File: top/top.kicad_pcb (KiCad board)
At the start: 4 copper layers, 28.3 x 40 mm, 23 parts, among them P1 CONN_10, P2 CONN_5, P3 CONN_20, U1 IQS572, U4 ESD

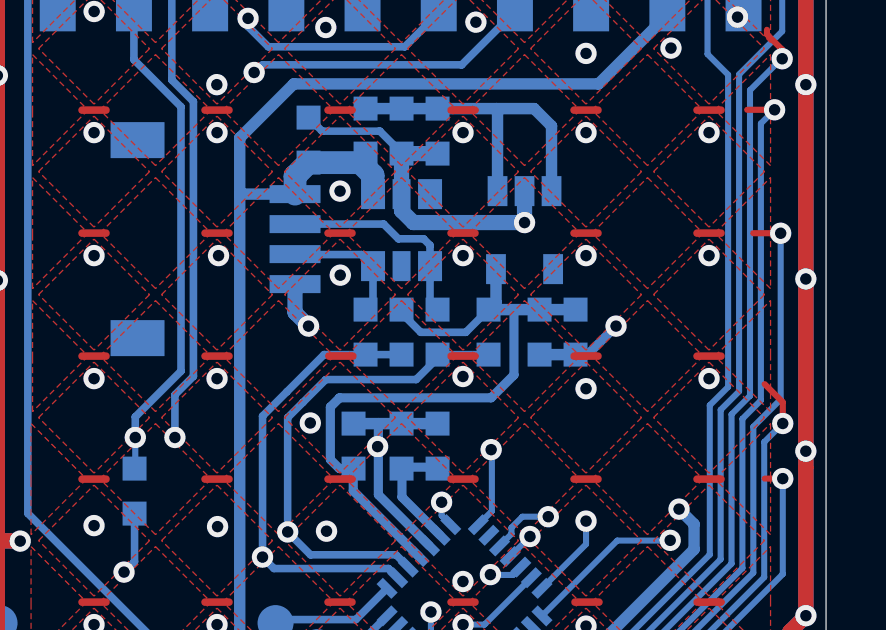
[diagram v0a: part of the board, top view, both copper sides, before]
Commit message: Remove redundant I2C pull-up resistors.
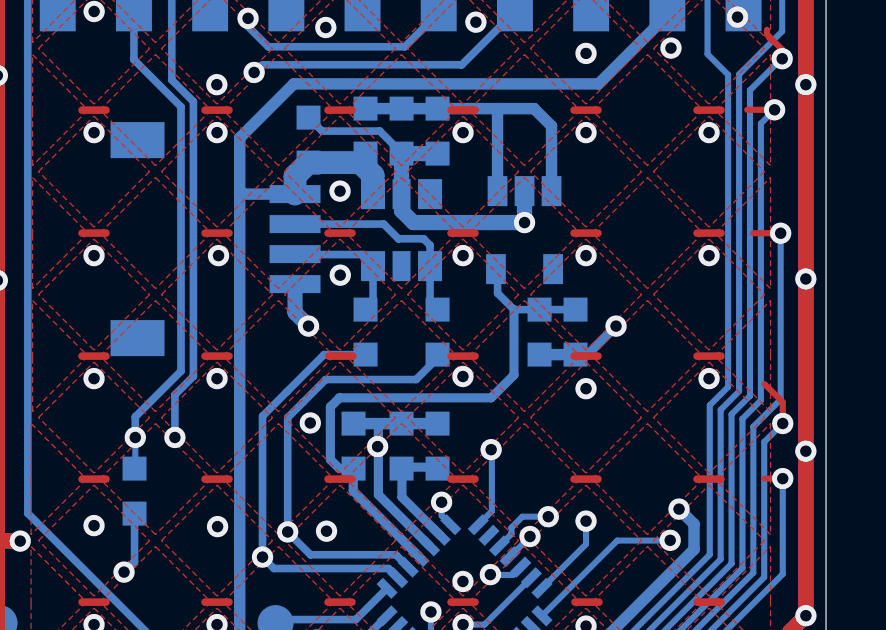
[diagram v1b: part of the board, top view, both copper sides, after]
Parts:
- removed R1, R2: 2.2K, ugl:SM0603
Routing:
- net +3V3: track 23.3 -> 18.4 mm
- net /SCL: track 56.0 -> 54.3 mm
- net /SDA: track 52.8 -> 51.4 mm
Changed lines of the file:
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@@
-(kicad_pcb (version 20171130) (host pcbnew 5.1.5-52549c5~84~ubuntu18.04.1)
+(kicad_pcb (version 20171130) (host pcbnew 5.1.5-52549c5~86~ubuntu18.04.1)
   (general
     (thickness 1.6)
     (drawings 75)
-    (tracks 759)
+    (tracks 756)
     (zones 0)
-    (modules 23)
+    (modules 21)
     (nets 53)
   )
@@
   )
   (layers
-    (0 F.Cu mixed hide)
+    (0 F.Cu mixed)
     (1 In1.Cu signal hide)
     (2 In2.Cu signal hide)
@@
     (46 B.CrtYd user)
     (47 F.CrtYd user)
-    (48 B.Fab user hide)
-    (49 F.Fab user hide)
+    (48 B.Fab user)
+    (49 F.Fab user)
   )
   (setup
-    (last_trace_width 0.2032)
+    (last_trace_width 0.254)
     (user_trace_width 0.2032)
     (user_trace_width 0.254)
@@
     (pad 2 smd rect (at 0.75 0 270) (size 0.8 0.8) (layers B.Cu B.Paste B.Mask)
       (net 4 /VCC_BOTTOM))
-    (model smd\resistors\R0603.wrl
-      (offset (xyz 0 0 0.02540000082496551))
-      (scale (xyz 0.5 0.5 0.5))
-      (rotate (xyz 0 0 0))
-    )
-  )
-  (module ugl:SM0603 (layer B.Cu)
-    (at 208.6 141.7 90)
-    (attr smd)
-    (fp_text reference R1 (at -3.08 1.8898 180) (layer B.SilkS)
-      (effects (font (size 0.75 0.75) (thickness 0.15)) (justify mirror))
-    )
-    (fp_text value 2.2K (at -4.2 2.4) (layer B.SilkS)
-      (effects (font (size 0.75 0.75) (thickness 0.15)) (justify mirror))
-    )
-    (fp_line (start 0.4 -0.5) (end -0.4 -0.5) (layer B.SilkS) (width 0.127))
-    (fp_line (start -0.4 0.5) (end 0.4 0.5) (layer B.SilkS) (width 0.127))
-    (pad 2 smd rect (at 0.75 0 90) (size 0.8 0.8) (layers B.Cu B.Paste B.Mask)
-      (net 12 +3V3))
-    (pad 1 smd rect (at -0.75 0 90) (size 0.8 0.8) (layers B.Cu B.Paste B.Mask)
-      (net 8 /SCL))
-    (model smd\resistors\R0603.wrl
-      (offset (xyz 0 0 0.02540000082496551))
-      (scale (xyz 0.5 0.5 0.5))
-      (rotate (xyz 0 0 0))
-    )
-  )
-  (module ugl:SM0603 (layer B.Cu)
-    (at 205.7 141.7 90)
-    (attr smd)
-    (fp_text reference R2 (at -3.7404 -6.6 270) (layer B.SilkS)
-      (effects (font (size 0.75 0.75) (thickness 0.15)) (justify mirror))
-    )
-    (fp_text value 2.2K (at -6.3 -6.6 90) (layer B.SilkS)
-      (effects (font (size 0.75 0.75) (thickness 0.15)) (justify mirror))
-    )
-    (fp_line (start -0.4 0.5) (end 0.4 0.5) (layer B.SilkS) (width 0.127))
-    (fp_line (start 0.4 -0.5) (end -0.4 -0.5) (layer B.SilkS) (width 0.127))
-    (pad 1 smd rect (at -0.75 0 90) (size 0.8 0.8) (layers B.Cu B.Paste B.Mask)
-      (net 11 /SDA))
-    (pad 2 smd rect (at 0.75 0 90) (size 0.8 0.8) (layers B.Cu B.Paste B.Mask)
-      (net 12 +3V3))
     (model smd\resistors\R0603.wrl
       (offset (xyz 0 0 0.02540000082496551))
@@
   (segment (start 200.25 131.55) (end 200.9 130.9) (width 0.2032) (layer In2.Cu) (net 8))
   (via (at 198.0946 157.8356) (size 0.635) (drill 0.381) (layers F.Cu B.Cu) (net 8))
-  (segment (start 208.6 142.45) (end 206.9 142.45) (width 0.254) (layer B.Cu) (net 8))
   (via (at 201.9046 148.3614) (size 0.7112) (drill 0.381) (layers F.Cu B.Cu) (net 8))
   (segment (start 198.57 157.5126) (end 198.0946 157.988) (width 0.3048) (layer B.Cu) (net 8))
@@
   (segment (start 198.57 156.1664) (end 198.0184 156.718) (width 0.3048) (layer B.Cu) (net 11))
   (segment (start 198.57 156.165) (end 198.57 156.1664) (width 0.3048) (layer B.Cu) (net 11))
-  (segment (start 205.7 142.45) (end 203.117 142.45) (width 0.254) (layer B.Cu) (net 11))
   (segment (start 203.117 142.45) (end 201.8792 143.6878) (width 0.254) (layer B.Cu) (net 11))
   (segment (start 201.0664 144.5006) (end 201.0664 149.1996) (width 0.254) (layer B.Cu) (net 11))
@@
   (segment (start 201.0664 133.3246) (end 200.787 133.0452) (width 0.254) (layer In1.Cu) (net 11))
   (segment (start 201.0664 149.1996) (end 201.0664 133.3246) (width 0.254) (layer In1.Cu) (net 11))
-  (segment (start 208.8475 140.7025) (end 208.6 140.95) (width 0.381) (layer B.Cu) (net 12))
-  (segment (start 208.8475 139.6) (end 208.8475 140.7025) (width 0.381) (layer B.Cu) (net 12))
-  (segment (start 205.7 141.066602) (end 206.339998 141.7066) (width 0.254) (layer B.Cu) (net 12))
-  (segment (start 205.7 140.95) (end 205.7 141.066602) (width 0.254) (layer B.Cu) (net 12))
-  (segment (start 207.8434 141.7066) (end 208.6 140.95) (width 0.254) (layer B.Cu) (net 12))
-  (segment (start 206.339998 141.7066) (end 207.8434 141.7066) (width 0.254) (layer B.Cu) (net 12))
+  (segment (start 203.117 142.45) (end 204.25 142.45) (width 0.254) (layer B.Cu) (net 11))
+  (segment (start 204.25 142.45) (end 204.3 142.5) (width 0.254) (layer B.Cu) (net 11))
   (segment (start 204.089 146.989) (end 206.27972 149.17972) (width 0.3048) (layer B.Cu) (net 12))
   (segment (start 204.089 146.177) (end 204.089 146.989) (width 0.3048) (layer B.Cu) (net 12))
@@
   (segment (start 208.6864 143.891) (end 203.6318 143.891) (width 0.3048) (layer B.Cu) (net 12))
   (segment (start 209.4484 143.129) (end 209.4484 140.95) (width 0.3048) (layer B.Cu) (net 12))
-  (segment (start 211.45 140.95) (end 209.4484 140.95) (width 0.381) (layer B.Cu) (net 12))
-  (segment (start 209.4484 140.95) (end 208.6 140.95) (width 0.381) (layer B.Cu) (net 12))
+  (segment (start 209.4484 140.95) (end 210.05 140.95) (width 0.254) (layer B.Cu) (net 12))
+  (segment (start 210.05 140.95) (end 210.1 140.9) (width 0.254) (layer B.Cu) (net 12))
+  (segment (start 209.4484 140.95) (end 208.9 140.4016) (width 0.254) (layer B.Cu) (net 12))
+  (segment (start 208.9 140.4016) (end 208.9 140) (width 0.254) (layer B.Cu) (net 12))
+  (segment (start 210.3 140.95) (end 211.45 140.95) (width 0.254) (layer B.Cu) (net 12))
   (segment (start 206.9146 146.2024) (end 205.7146 146.2024) (width 0.3048) (layer B.Cu) (net 14))
   (segment (start 205.7146 147.200387) (end 205.7146 146.2278) (width 0.3048) (layer B.Cu) (net 14))

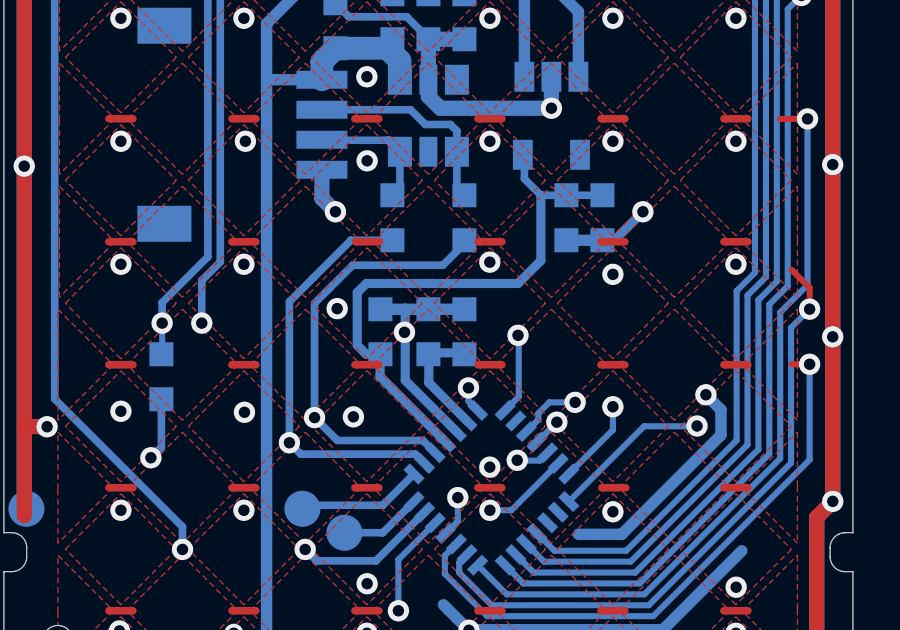
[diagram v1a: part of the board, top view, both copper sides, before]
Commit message: Move bypass caps closer to pin 4.
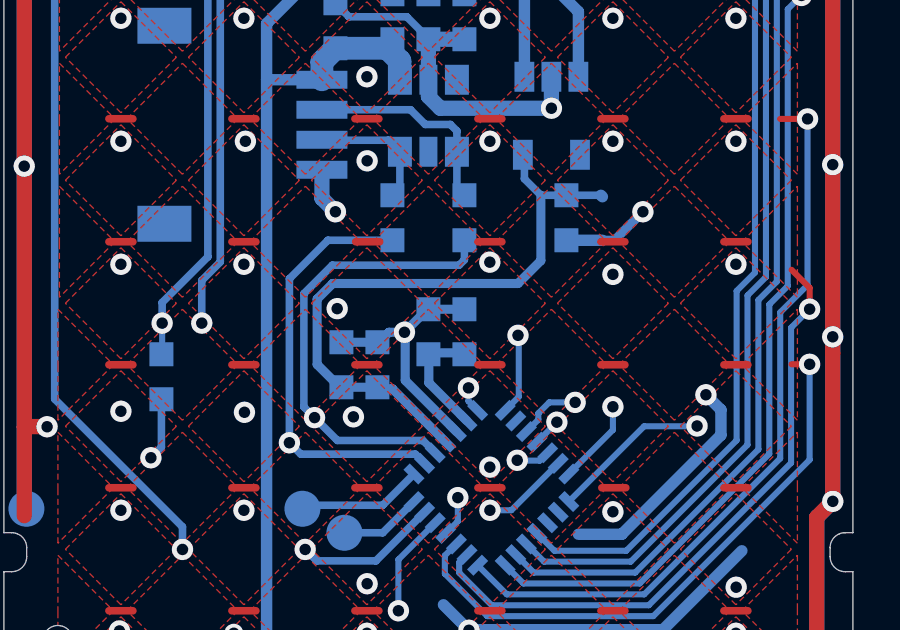
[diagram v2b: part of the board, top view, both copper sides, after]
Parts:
- moved C6 9.98 mm to (202.8, 146.6), turned to 270 degrees
- moved C5 1.10 mm to (204.0, 146.6)
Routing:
- net +3V3: track 18.4 -> 20.4 mm
- net /SCL: track 54.3 -> 55.3 mm
- net GND: track 449.5 -> 450.1 mm
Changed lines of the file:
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@@
     (thickness 1.6)
     (drawings 75)
-    (tracks 756)
+    (tracks 759)
     (zones 0)
     (modules 21)
@@
   )
   (setup
-    (last_trace_width 0.254)
+    (last_trace_width 0.3048)
     (user_trace_width 0.2032)
     (user_trace_width 0.254)
@@
   )
   (module ugl:SM0603 (layer B.Cu)
-    (at 204.1 145.5 270)
+    (at 204 146.6 270)
     (attr smd)
     (fp_text reference C5 (at 0.6262 2.17 270) (layer B.SilkS)
@@
   )
   (module ugl:SM0603 (layer B.Cu)
-    (at 211.5 141.7 90)
+    (at 202.8 146.6 270)
     (attr smd)
     (fp_text reference C6 (at 1.3 1.1742 270) (layer B.SilkS)
@@
     (fp_line (start -0.4 0.5) (end 0.4 0.5) (layer B.SilkS) (width 0.127))
     (fp_line (start 0.4 -0.5) (end -0.4 -0.5) (layer B.SilkS) (width 0.127))
-    (pad 1 smd rect (at -0.75 0 90) (size 0.8 0.8) (layers B.Cu B.Paste B.Mask)
-      (net 1 GND))
-    (pad 2 smd rect (at 0.75 0 90) (size 0.8 0.8) (layers B.Cu B.Paste B.Mask)
+    (pad 1 smd rect (at -0.75 0 270) (size 0.8 0.8) (layers B.Cu B.Paste B.Mask)
+      (net 1 GND))
+    (pad 2 smd rect (at 0.75 0 270) (size 0.8 0.8) (layers B.Cu B.Paste B.Mask)
       (net 12 +3V3))
     (model smd\resistors\R0603.wrl
@@
   (segment (start 204.9272 147.120093) (end 204.9272 145.288) (width 0.3048) (layer B.Cu) (net 1))
   (segment (start 206.633274 148.826167) (end 204.9272 147.120093) (width 0.3048) (layer B.Cu) (net 1))
-  (segment (start 204.5 144.75) (end 204.9272 144.75) (width 0.381) (layer B.Cu) (net 1))
   (via (at 204.9018 145.5166) (size 0.7112) (drill 0.381) (layers F.Cu B.Cu) (net 1))
-  (segment (start 204.9272 144.75) (end 206.9 144.75) (width 0.381) (layer B.Cu) (net 1))
-  (segment (start 204.9272 144.7546) (end 204.9018 144.7292) (width 0.3048) (layer B.Cu) (net 1))
-  (segment (start 204.9272 145.288) (end 204.9272 144.7546) (width 0.3048) (layer B.Cu) (net 1))
   (segment (start 192.2272 121.412) (end 192.2272 122.0724) (width 0.508) (layer B.Cu) (net 1))
   (segment (start 194.4878 119.1514) (end 192.2272 121.412) (width 0.508) (layer B.Cu) (net 1))
@@
   (segment (start 214.95 147.6) (end 214.95 147.6) (width 0.381) (layer B.Cu) (net 1))
   (via (at 214.95 147.6) (size 0.7112) (drill 0.381) (layers F.Cu B.Cu) (net 1))
+  (segment (start 204.3834 145.5166) (end 204.3 145.6) (width 0.3048) (layer B.Cu) (net 1))
+  (segment (start 204.9018 145.5166) (end 205.4 145.0184) (width 0.3048) (layer B.Cu) (net 1))
+  (segment (start 205.7 144.75) (end 206.75 144.75) (width 0.3048) (layer B.Cu) (net 1))
+  (segment (start 206.75 144.75) (end 206.8 144.8) (width 0.3048) (layer B.Cu) (net 1))
+  (segment (start 204.9018 145.5166) (end 204.3834 145.5166) (width 0.3048) (layer B.Cu) (net 1))
+  (segment (start 202.8 145.85) (end 203.85 145.85) (width 0.3048) (layer B.Cu) (net 1))
+  (segment (start 203.85 145.85) (end 203.9 145.9) (width 0.3048) (layer B.Cu) (net 1))
   (segment (start 206.65 140.7) (end 206.9 140.95) (width 0.254) (layer B.Cu) (net 2))
   (segment (start 206.65 139.5) (end 206.65 140.7) (width 0.254) (layer B.Cu) (net 2))
@@
   (segment (start 198.57 157.5126) (end 198.0946 157.988) (width 0.3048) (layer B.Cu) (net 8))
   (segment (start 198.57 157.435) (end 198.57 157.5126) (width 0.3048) (layer B.Cu) (net 8))
-  (segment (start 206.9 142.566602) (end 206.9 142.45) (width 0.254) (layer B.Cu) (net 8))
-  (segment (start 206.185202 143.2814) (end 206.9 142.566602) (width 0.254) (layer B.Cu) (net 8))
-  (segment (start 203.1746 143.2814) (end 206.185202 143.2814) (width 0.254) (layer B.Cu) (net 8))
-  (segment (start 202.4126 144.0434) (end 203.1746 143.2814) (width 0.254) (layer B.Cu) (net 8))
-  (segment (start 201.9046 144.5514) (end 201.9046 148.3614) (width 0.254) (layer B.Cu) (net 8))
-  (segment (start 202.4126 144.0434) (end 201.9046 144.5514) (width 0.254) (layer B.Cu) (net 8))
   (segment (start 202.6666 149.1234) (end 201.9046 148.3614) (width 0.254) (layer B.Cu) (net 8))
   (segment (start 205.926167 149.533274) (end 205.516293 149.1234) (width 0.254) (layer B.Cu) (net 8))
@@
   (segment (start 200.8378 155.855698) (end 200.8378 150.7744) (width 0.254) (layer In1.Cu) (net 8))
   (segment (start 200.8378 150.7744) (end 201.9046 149.7076) (width 0.254) (layer In1.Cu) (net 8))
+  (segment (start 201.549001 148.005801) (end 201.549001 144.229127) (width 0.254) (layer B.Cu) (net 8))
+  (segment (start 201.549001 144.229127) (end 202.496728 143.2814) (width 0.254) (layer B.Cu) (net 8))
+  (segment (start 201.9046 148.3614) (end 201.549001 148.005801) (width 0.254) (layer B.Cu) (net 8))
+  (segment (start 202.496728 143.2814) (end 206.7226 143.2814) (width 0.254) (layer B.Cu) (net 8))
+  (segment (start 206.7226 143.2814) (end 206.9 143.104) (width 0.254) (layer B.Cu) (net 8))
+  (segment (start 206.9 143.104) (end 206.9 142.45) (width 0.254) (layer B.Cu) (net 8))
   (segment (start 208.9 134.2748) (end 208.9 137) (width 0.381) (layer B.Cu) (net 9))
   (segment (start 204.5 134.25) (end 208.8752 134.25) (width 0.381) (layer B.Cu) (net 9))
@@
   (segment (start 198.57 156.1664) (end 198.0184 156.718) (width 0.3048) (layer B.Cu) (net 11))
   (segment (start 198.57 156.165) (end 198.57 156.1664) (width 0.3048) (layer B.Cu) (net 11))
-  (segment (start 203.117 142.45) (end 201.8792 143.6878) (width 0.254) (layer B.Cu) (net 11))
-  (segment (start 201.0664 144.5006) (end 201.0664 149.1996) (width 0.254) (layer B.Cu) (net 11))
-  (segment (start 201.8792 143.6878) (end 201.0664 144.5006) (width 0.254) (layer B.Cu) (net 11))
   (segment (start 201.4474 149.5806) (end 201.0664 149.1996) (width 0.254) (layer B.Cu) (net 11))
   (segment (start 205.572614 149.886827) (end 205.266387 149.5806) (width 0.254) (layer B.Cu) (net 11))
@@
   (segment (start 201.0664 133.3246) (end 200.787 133.0452) (width 0.254) (layer In1.Cu) (net 11))
   (segment (start 201.0664 149.1996) (end 201.0664 133.3246) (width 0.254) (layer In1.Cu) (net 11))
-  (segment (start 203.117 142.45) (end 204.25 142.45) (width 0.254) (layer B.Cu) (net 11))
-  (segment (start 204.25 142.45) (end 204.3 142.5) (width 0.254) (layer B.Cu) (net 11))
-  (segment (start 204.089 146.989) (end 206.27972 149.17972) (width 0.3048) (layer B.Cu) (net 12))
-  (segment (start 204.089 146.177) (end 204.089 146.989) (width 0.3048) (layer B.Cu) (net 12))
+  (segment (start 201.0664 143.7336) (end 201.0664 149.1996) (width 0.254) (layer B.Cu) (net 11))
+  (segment (start 204.3 142.5) (end 204.25 142.45) (width 0.254) (layer B.Cu) (net 11))
+  (segment (start 202.35 142.45) (end 201.0664 143.7336) (width 0.254) (layer B.Cu) (net 11))
+  (segment (start 204.25 142.45) (end 202.35 142.45) (width 0.254) (layer B.Cu) (net 11))
   (segment (start 211.5 141) (end 211.45 140.95) (width 0.381) (layer B.Cu) (net 12))
-  (segment (start 203.6286 146.25) (end 204.1 146.25) (width 0.3048) (layer B.Cu) (net 12))
-  (segment (start 203.327 145.9484) (end 203.6286 146.25) (width 0.3048) (layer B.Cu) (net 12))
-  (segment (start 203.327 144.1958) (end 203.327 145.9484) (width 0.3048) (layer B.Cu) (net 12))
-  (segment (start 203.6318 143.891) (end 203.327 144.1958) (width 0.3048) (layer B.Cu) (net 12))
   (segment (start 209.4484 143.129) (end 208.6864 143.891) (width 0.3048) (layer B.Cu) (net 12))
-  (segment (start 208.6864 143.891) (end 203.6318 143.891) (width 0.3048) (layer B.Cu) (net 12))
   (segment (start 209.4484 143.129) (end 209.4484 140.95) (width 0.3048) (layer B.Cu) (net 12))
   (segment (start 209.4484 140.95) (end 210.05 140.95) (width 0.254) (layer B.Cu) (net 12))
@@
   (segment (start 208.9 140.4016) (end 208.9 140) (width 0.254) (layer B.Cu) (net 12))
   (segment (start 210.3 140.95) (end 211.45 140.95) (width 0.254) (layer B.Cu) (net 12))
+  (segment (start 206.27972 149.17972) (end 204.5 147.4) (width 0.3048) (layer B.Cu) (net 12))
+  (segment (start 204.5 147.4) (end 204 147.4) (width 0.3048) (layer B.Cu) (net 12))
+  (segment (start 204 147.35) (end 202.95 147.35) (width 0.3048) (layer B.Cu) (net 12))
+  (segment (start 202.95 147.35) (end 202.9 147.4) (width 0.3048) (layer B.Cu) (net 12))
+  (segment (start 201.990989 144.408559) (end 201.990989 146.590989) (width 0.3048) (layer B.Cu) (net 12))
+  (segment (start 202.508548 143.891) (end 201.990989 144.408559) (width 0.3048) (layer B.Cu) (net 12))
+  (segment (start 208.6864 143.891) (end 202.508548 143.891) (width 0.3048) (layer B.Cu) (net 12))
+  (segment (start 201.990989 146.590989) (end 202.6 147.2) (width 0.3048) (layer B.Cu) (net 12))
   (segment (start 206.9146 146.2024) (end 205.7146 146.2024) (width 0.3048) (layer B.Cu) (net 14))
   (segment (start 205.7146 147.200387) (end 205.7146 146.2278) (width 0.3048) (layer B.Cu) (net 14))
